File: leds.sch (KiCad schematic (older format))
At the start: 66 parts

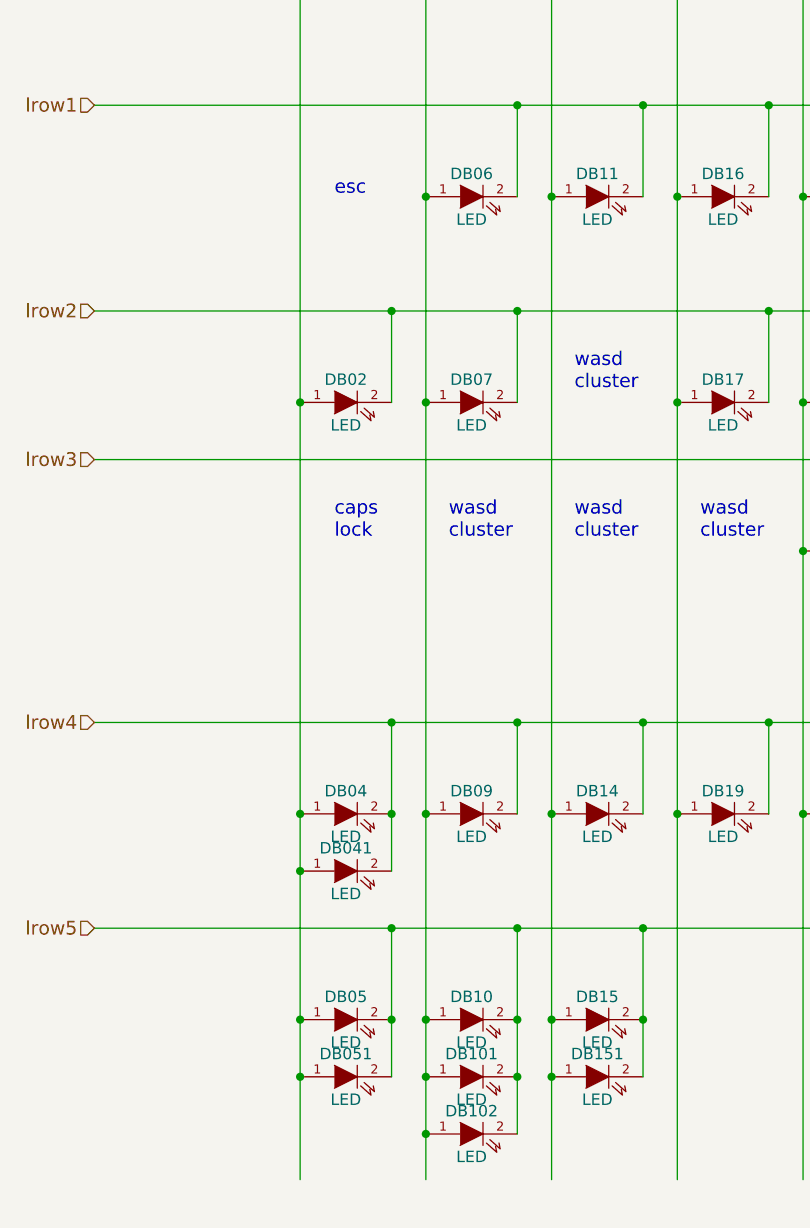
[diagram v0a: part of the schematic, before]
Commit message: 修改usb接口为type c
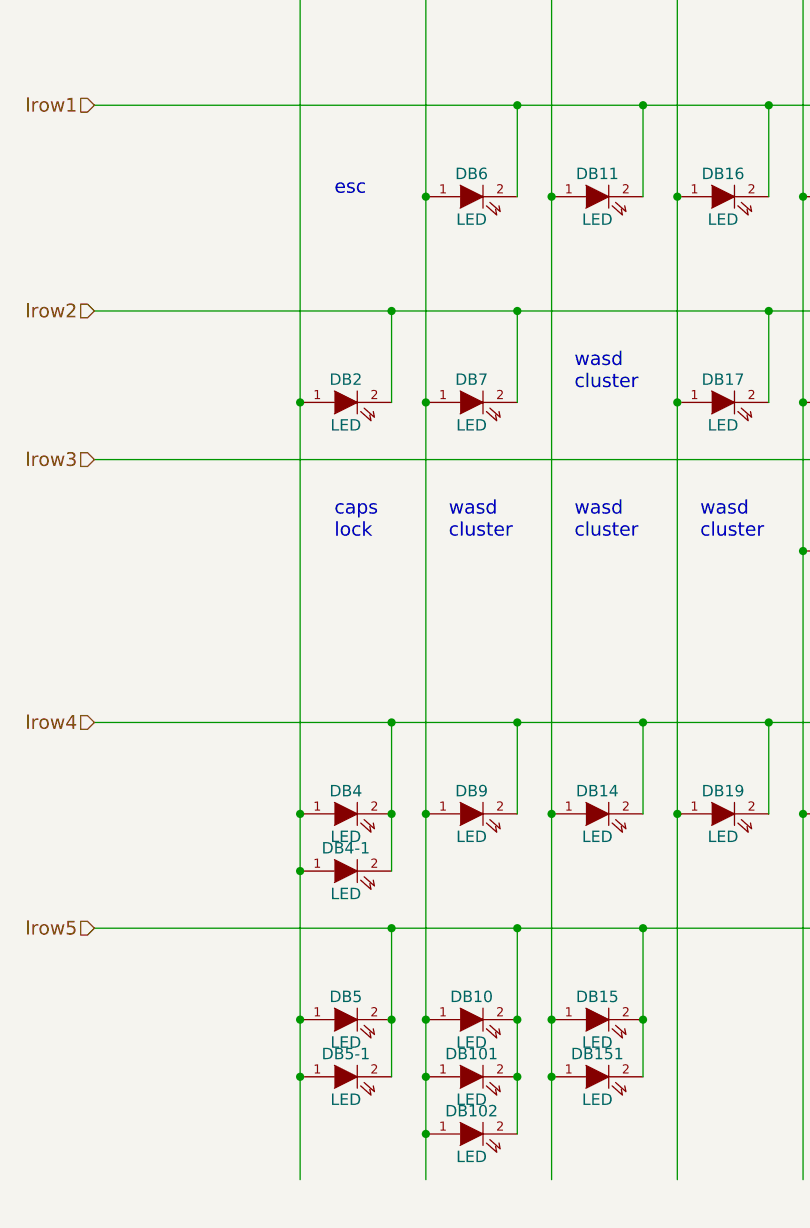
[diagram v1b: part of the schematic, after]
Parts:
- renumbered DB02 to DB2, DB04 to DB4, DB041 to DB4-1, DB05 to DB5, DB051 to DB5-1, DB06 to DB6, DB07 to DB7, DB09 to DB9
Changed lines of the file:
@@
 LIBS:device
 LIBS:conn
+LIBS:usb-type-c
 LIBS:keyboard-cache
 EELAYER 25 0
@@
 $Descr A4 11693 8268
 encoding utf-8
-Sheet 3 3
+Sheet 3 4
 Title ""
 Date "17 jul 2013"
@@
 $EndComp
 $Comp
-L LED DB06
+L LED DB6
 U 1 1 5190074C
 P 2800 1950
-F 0 "DB06" H 2800 2050 50  0000 C CNN
+F 0 "DB6" H 2800 2050 50  0000 C CNN
 F 1 "LED" H 2800 1850 50  0000 C CNN
 F 2 "mx1a:MX1A-led_no3d" H 2800 1950 60  0001 C CNN
@@
 $EndComp
 $Comp
-L LED DB02
+L LED DB2
 U 1 1 519007B5
 P 2250 2850
-F 0 "DB02" H 2250 2950 50  0000 C CNN
+F 0 "DB2" H 2250 2950 50  0000 C CNN
 F 1 "LED" H 2250 2750 50  0000 C CNN
 F 2 "mx1a:MX1A-led_no3d" H 2250 2850 60  0001 C CNN
@@
 $EndComp
 $Comp
-L LED DB07
+L LED DB7
 U 1 1 519007BC
 P 2800 2850
-F 0 "DB07" H 2800 2950 50  0000 C CNN
+F 0 "DB7" H 2800 2950 50  0000 C CNN
 F 1 "LED" H 2800 2750 50  0000 C CNN
 F 2 "mx1a:MX1A-led_no3d" H 2800 2850 60  0001 C CNN
@@
 $EndComp
 $Comp
-L LED DB04
+L LED DB4
 U 1 1 51900887
 P 2250 4650
-F 0 "DB04" H 2250 4750 50  0000 C CNN
+F 0 "DB4" H 2250 4750 50  0000 C CNN
 F 1 "LED" H 2250 4550 50  0000 C CNN
 F 2 "mx1a:MX1A-led_no3d" H 2250 4650 60  0001 C CNN
@@
 $EndComp
 $Comp
-L LED DB09
+L LED DB9
 U 1 1 5190088E
 P 2800 4650
-F 0 "DB09" H 2800 4750 50  0000 C CNN
+F 0 "DB9" H 2800 4750 50  0000 C CNN
 F 1 "LED" H 2800 4550 50  0000 C CNN
 F 2 "mx1a:MX1A-led_no3d" H 2800 4650 60  0001 C CNN
@@
 $EndComp
 $Comp
-L LED DB05
+L LED DB5
 U 1 1 519008F0
 P 2250 5550
-F 0 "DB05" H 2250 5650 50  0000 C CNN
+F 0 "DB5" H 2250 5650 50  0000 C CNN
 F 1 "LED" H 2250 5450 50  0000 C CNN
 F 2 "" H 2250 5550 60  0001 C CNN
@@
 $EndComp
 $Comp
-L LED DB051
+L LED DB5-1
 U 1 1 51C0378E
 P 2250 5800
-F 0 "DB051" H 2250 5900 50  0000 C CNN
+F 0 "DB5-1" H 2250 5900 50  0000 C CNN
 F 1 "LED" H 2250 5700 50  0000 C CNN
 F 2 "" H 2250 5800 60  0001 C CNN
@@
 Fn
 $Comp
-L LED DB041
+L LED DB4-1
 U 1 1 51D98243
 P 2250 4900
-F 0 "DB041" H 2250 5000 50  0000 C CNN
+F 0 "DB4-1" H 2250 5000 50  0000 C CNN
 F 1 "LED" H 2250 4800 50  0000 C CNN
 F 2 "mx1a:MX1A-led_no3d" H 2250 4900 60  0001 C CNN

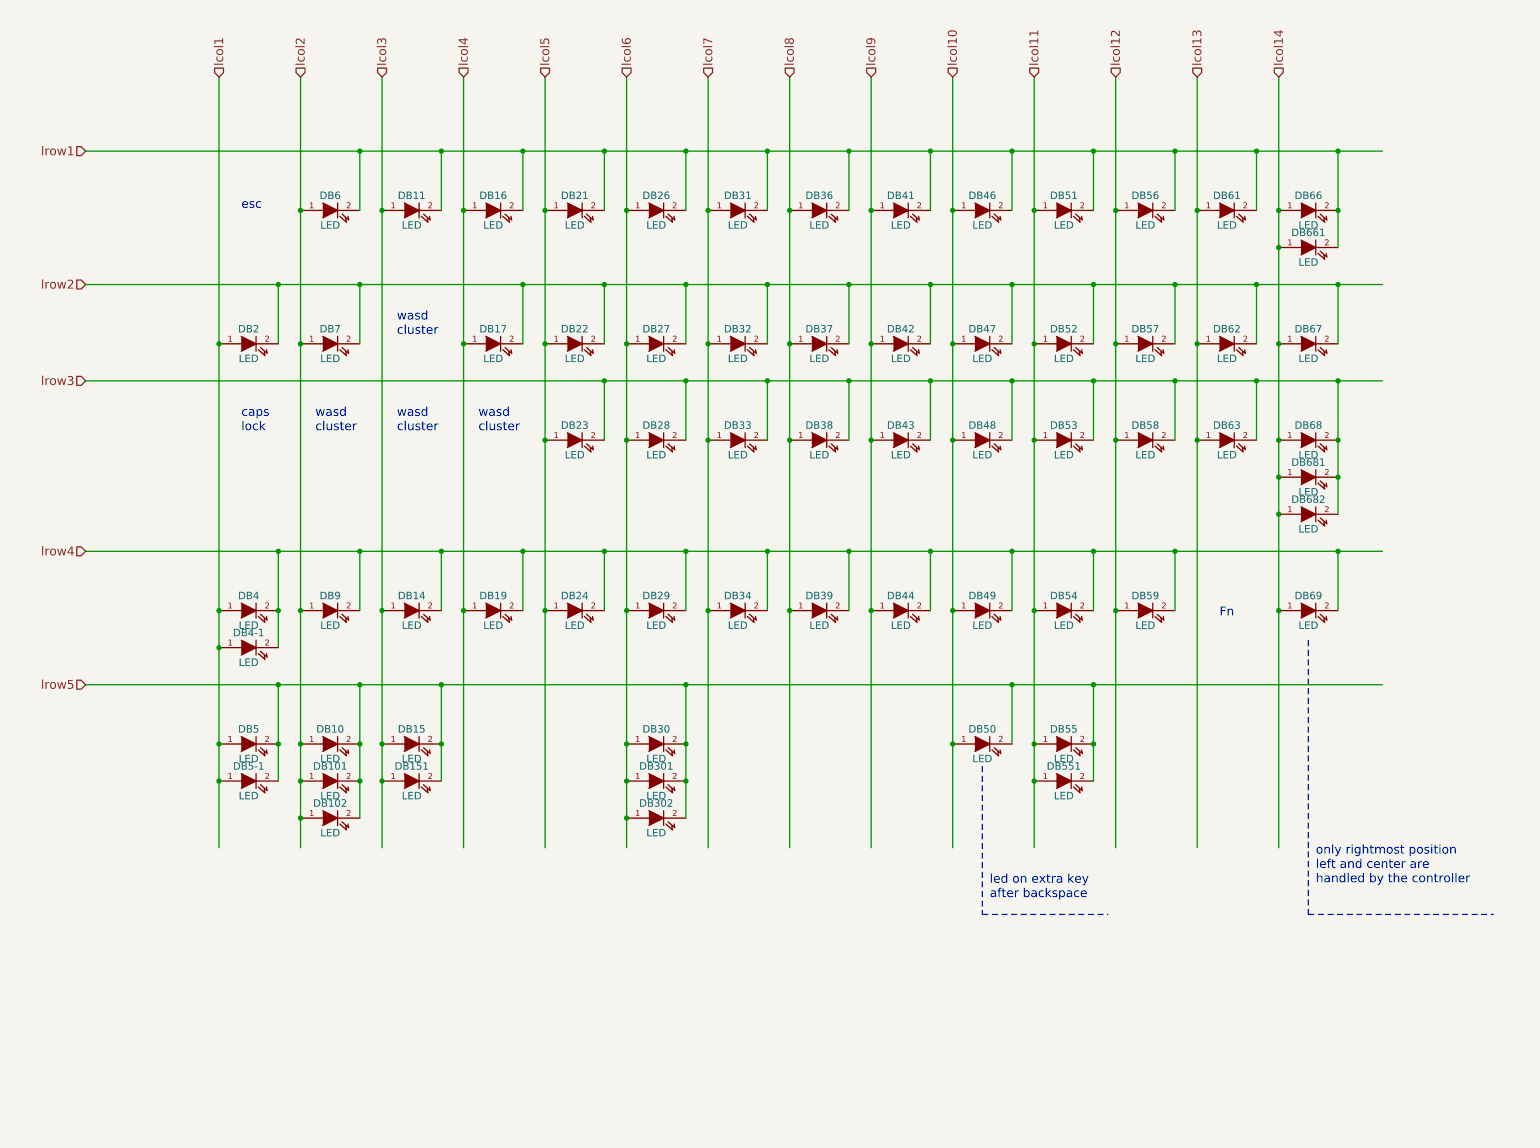
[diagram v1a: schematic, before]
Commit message: 增加一列F功能区 增加TrackPiont模块,同时增加ffc排线接口 右移右侧键布局
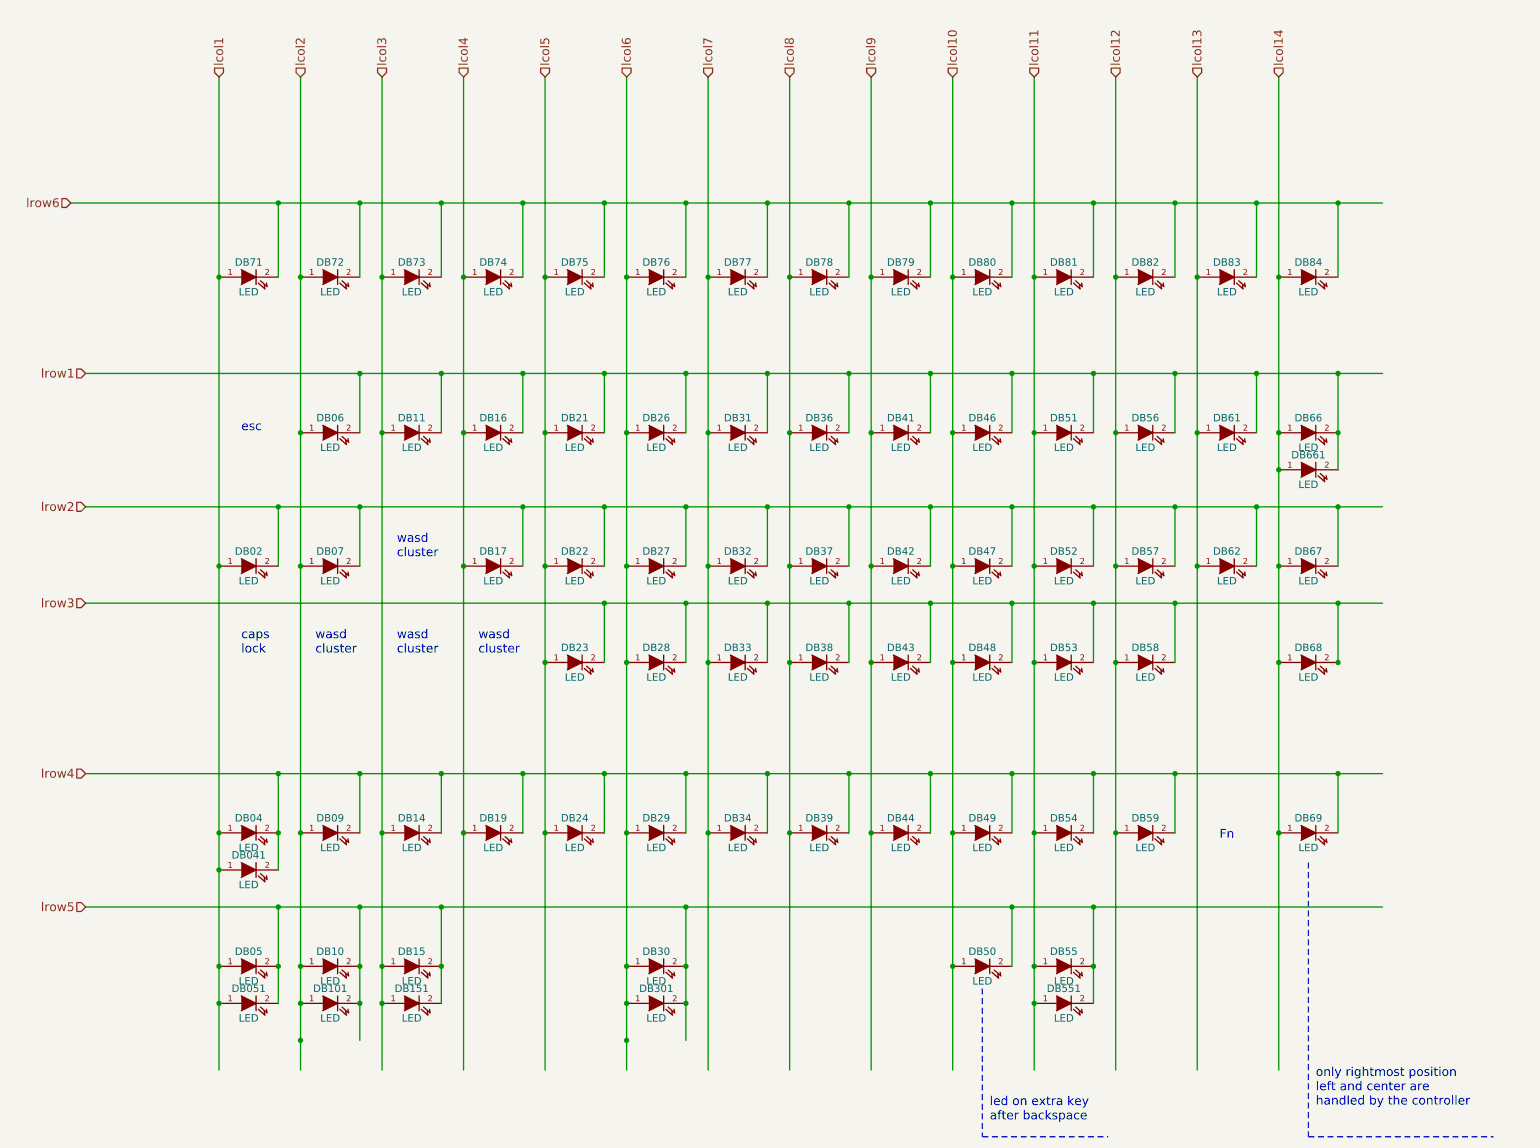
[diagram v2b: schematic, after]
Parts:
- removed DB102: LED, symbol LED
- removed DB302, DB63, DB681, DB682: LED, mx1a:MX1A-led_no3d, symbol LED
- added DB71, DB72, DB73, DB74, DB75, DB76, DB77, DB78, DB79, DB80, DB81, DB82, DB83, DB84: LED, mx1a:MX1A-led_no3d, symbol LED
- renumbered DB2 to DB02, DB4 to DB04, DB4-1 to DB041, DB5 to DB05, DB5-1 to DB051, DB6 to DB06, DB7 to DB07, DB9 to DB09
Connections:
- net labels added: lrow6
- wire segments 74 -> 88
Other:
- moved on the sheet: DB02, DB04, DB041, DB05, DB051, DB06, DB07, DB09, DB10, DB101, DB11, DB14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

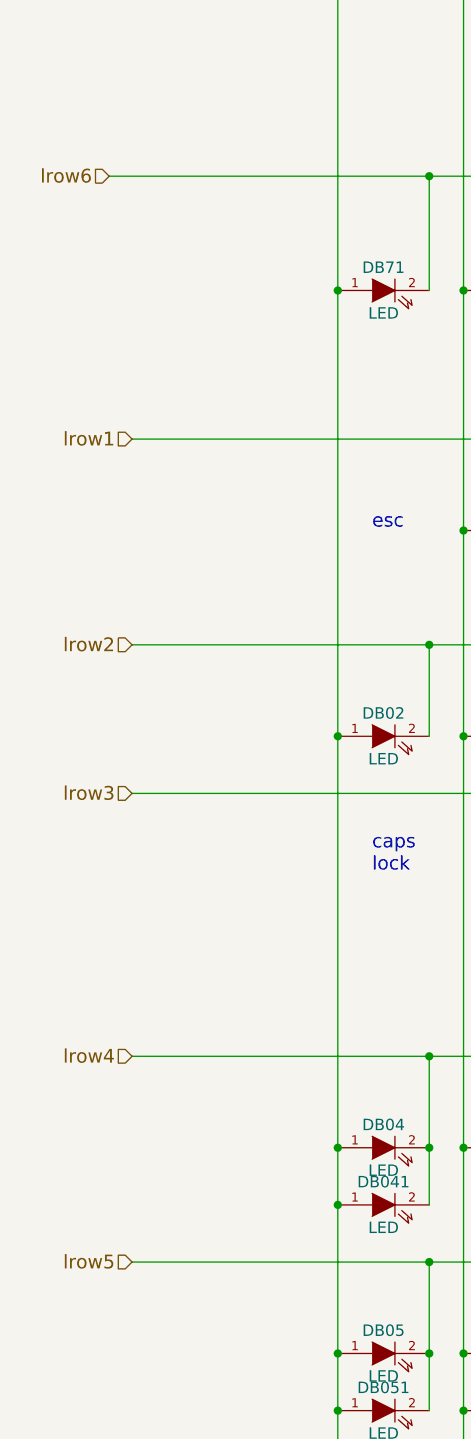
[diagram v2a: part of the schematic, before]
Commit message: 第一版 修改了鼠标三键错位 TrackPiont模块ffc接口位置修改方便连接
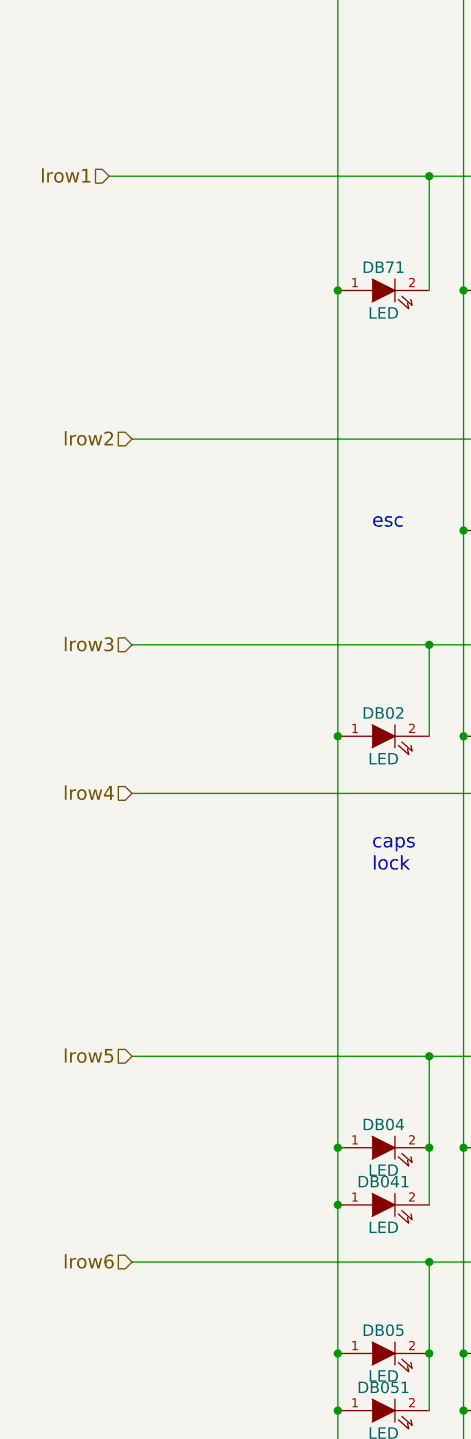
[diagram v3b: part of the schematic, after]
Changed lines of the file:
@@
 only rightmost position\nleft and center are\nhandled by the controller
 Text HLabel 1150 3050 0    60   Input ~ 0
-lrow1
+lrow2
 Text HLabel 1150 3950 0    60   Input ~ 0
-lrow2
+lrow3
 Text HLabel 1150 4600 0    60   Input ~ 0
-lrow3
+lrow4
 Text HLabel 1150 5750 0    60   Input ~ 0
-lrow4
+lrow5
 Text HLabel 1150 6650 0    60   Input ~ 0
-lrow5
+lrow6
 Text HLabel 2050 1050 1    60   Input ~ 0
 lcol1
@@
 $EndComp
 Text HLabel 1050 1900 0    60   Input ~ 0
-lrow6
+lrow1
 Wire Wire Line
 	4650 3050 4650 3450
